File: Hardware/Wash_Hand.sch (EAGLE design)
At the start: 91 parts, among them IC1 LM358D, IC2 LP298XS, IC3 405016TSSOP, J1 I2C, J2 ICSP, J3 SPI, J4 9V_CONN, J5 EXT_VCC, J6 6_PIN_SERIAL_CABLEPTH, J7 OP_B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

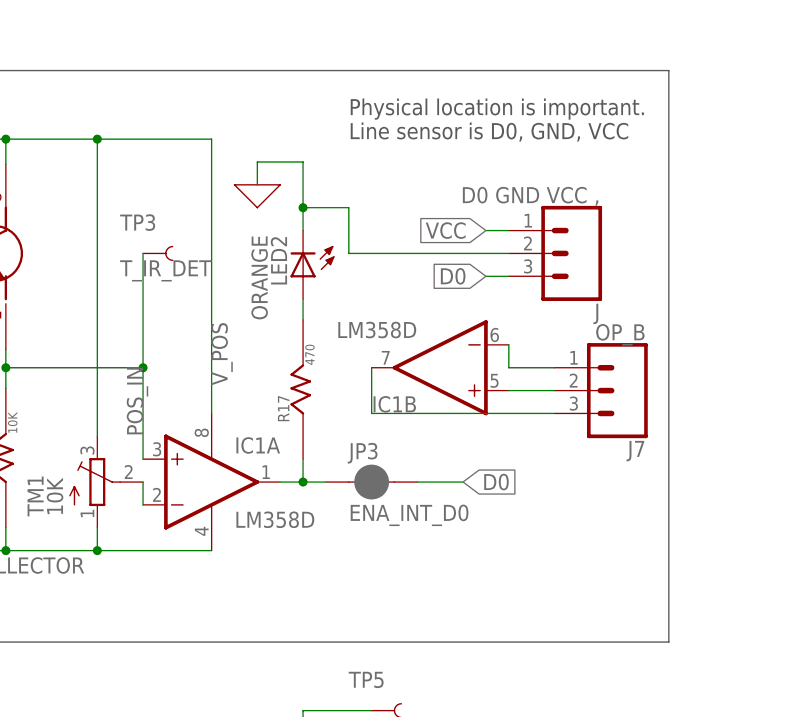
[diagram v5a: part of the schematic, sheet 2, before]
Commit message: Board/Schematic: Route Orange LED2 to NPN_COLLECTOR
instead of the common ground. This way when we disable
the ON_OFF_SWT the light will not be light up.

Signed-off-by: Konrad Rzeszutek Wilk <konrad@kernel.org>
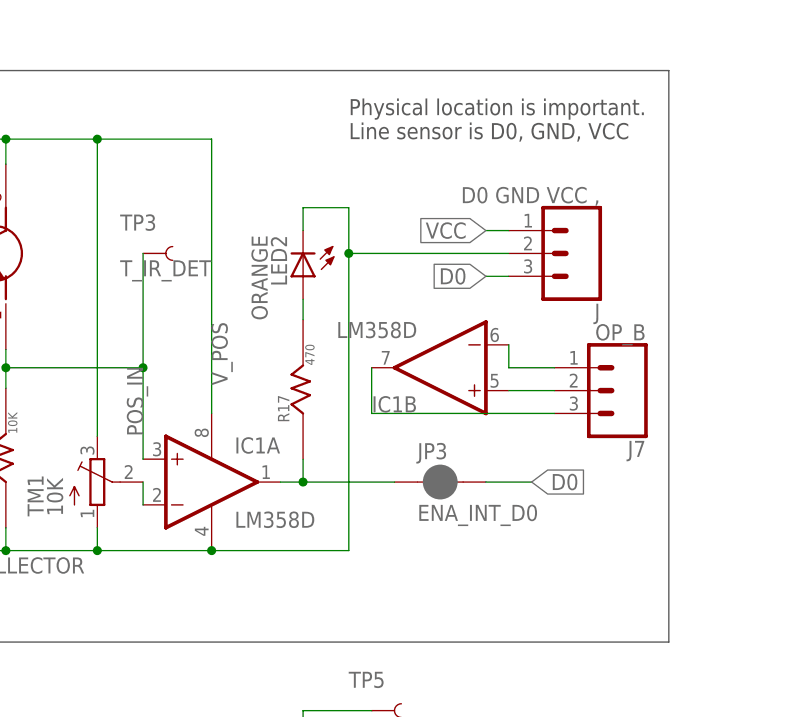
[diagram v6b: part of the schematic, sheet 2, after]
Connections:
- net 0: no longer J.2, LED2.C
- net NPN_COLLECTOR: now also J.2, LED2.C
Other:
- moved on the sheet: JP3
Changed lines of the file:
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@@
 <part name="LOGO2" library="darnok_logo" deviceset="HAPPY_FACE_LOGO" device=""/>
 <part name="X_1" library="ngspice-simulation" library_urn="urn:adsk.eagle:library:527439" deviceset="GND" device=""/>
-<part name="X_4" library="ngspice-simulation" library_urn="urn:adsk.eagle:library:527439" deviceset="GND" device=""/>
 <part name="JP7" library="SparkFun-Jumpers" library_urn="urn:adsk.eagle:library:528" deviceset="JUMPER-SMT_2_NO" device="_SILK" package3d_urn="urn:adsk.eagle:package:39279/1" value="BYPASS_SWT"/>
 </parts>
@@
 <attribute name="NAME" x="233.68" y="151.892" size="1.778" layer="95" font="vector" rot="R180"/>
 </instance>
-<instance part="JP3" gate="G$1" x="208.28" y="132.08" smashed="yes">
-<attribute name="NAME" x="205.74" y="134.62" size="1.778" layer="95" font="vector"/>
-<attribute name="VALUE" x="205.74" y="129.54" size="1.778" layer="96" font="vector" align="top-left"/>
+<instance part="JP3" gate="G$1" x="215.9" y="132.08" smashed="yes">
+<attribute name="NAME" x="213.36" y="134.62" size="1.778" layer="95" font="vector"/>
+<attribute name="VALUE" x="213.36" y="129.54" size="1.778" layer="96" font="vector" align="top-left"/>
 </instance>
 <instance part="JP4" gate="G$1" x="142.24" y="170.18" smashed="yes">
@@
 </instance>
 <instance part="X_1" gate="G$1" x="137.16" y="119.38" smashed="yes"/>
-<instance part="X_4" gate="G$1" x="195.58" y="165.1" smashed="yes"/>
 <instance part="JP7" gate="G$1" x="147.32" y="121.92" smashed="yes">
 <attribute name="NAME" x="144.78" y="124.46" size="1.778" layer="95" font="vector"/>
@@
 <junction x="137.16" y="121.92"/>
 </segment>
-<segment>
-<pinref part="X_4" gate="G$1" pin="0"/>
-<wire x1="195.58" y1="165.1" x2="195.58" y2="167.64" width="0.1524" layer="91"/>
-<pinref part="LED2" gate="G$1" pin="C"/>
-<wire x1="195.58" y1="167.64" x2="200.66" y2="167.64" width="0.1524" layer="91"/>
-<wire x1="200.66" y1="167.64" x2="200.66" y2="162.56" width="0.1524" layer="91"/>
-<pinref part="J" gate="J$1" pin="2"/>
-<wire x1="200.66" y1="162.56" x2="200.66" y2="160.02" width="0.1524" layer="91"/>
-<wire x1="223.52" y1="157.48" x2="205.74" y2="157.48" width="0.1524" layer="91"/>
-<wire x1="205.74" y1="157.48" x2="205.74" y2="162.56" width="0.1524" layer="91"/>
-<wire x1="205.74" y1="162.56" x2="200.66" y2="162.56" width="0.1524" layer="91"/>
-<junction x="200.66" y="162.56"/>
-</segment>
 </net>
 <net name="D0" class="0">
@@
 <wire x1="198.12" y1="132.08" x2="200.66" y2="132.08" width="0.1524" layer="91"/>
 <pinref part="R17" gate="G$1" pin="R_1"/>
-<wire x1="200.66" y1="132.08" x2="203.2" y2="132.08" width="0.1524" layer="91"/>
+<wire x1="200.66" y1="132.08" x2="210.82" y2="132.08" width="0.1524" layer="91"/>
 <wire x1="200.66" y1="132.08" x2="200.66" y2="134.62" width="0.1524" layer="91"/>
 <junction x="200.66" y="132.08"/>
@@
 <segment>
 <pinref part="JP3" gate="G$1" pin="2"/>
-<wire x1="213.36" y1="132.08" x2="218.44" y2="132.08" width="0.1524" layer="91"/>
-<label x="218.44" y="132.08" size="1.778" layer="95" xref="yes"/>
+<wire x1="220.98" y1="132.08" x2="226.06" y2="132.08" width="0.1524" layer="91"/>
+<label x="226.06" y="132.08" size="1.778" layer="95" xref="yes"/>
 </segment>
 </net>
@@
 <wire x1="152.4" y1="121.92" x2="154.94" y2="121.92" width="0.1524" layer="91"/>
 <wire x1="154.94" y1="121.92" x2="154.94" y2="124.46" width="0.1524" layer="91"/>
-</segment>
-</net>
+<pinref part="LED2" gate="G$1" pin="C"/>
+<pinref part="J" gate="J$1" pin="2"/>
+<wire x1="200.66" y1="162.56" x2="200.66" y2="160.02" width="0.1524" layer="91"/>
+<wire x1="223.52" y1="157.48" x2="205.74" y2="157.48" width="0.1524" layer="91"/>
+<wire x1="205.74" y1="157.48" x2="205.74" y2="162.56" width="0.1524" layer="91"/>
+<wire x1="205.74" y1="162.56" x2="200.66" y2="162.56" width="0.1524" layer="91"/>
+<wire x1="205.74" y1="157.48" x2="205.74" y2="124.46" width="0.1524" layer="91"/>
+<wire x1="205.74" y1="124.46" x2="190.5" y2="124.46" width="0.1524" layer="91"/>
+<junction x="205.74" y="157.48"/>
+<junction x="190.5" y="124.46"/>
+</segment>
+</net>

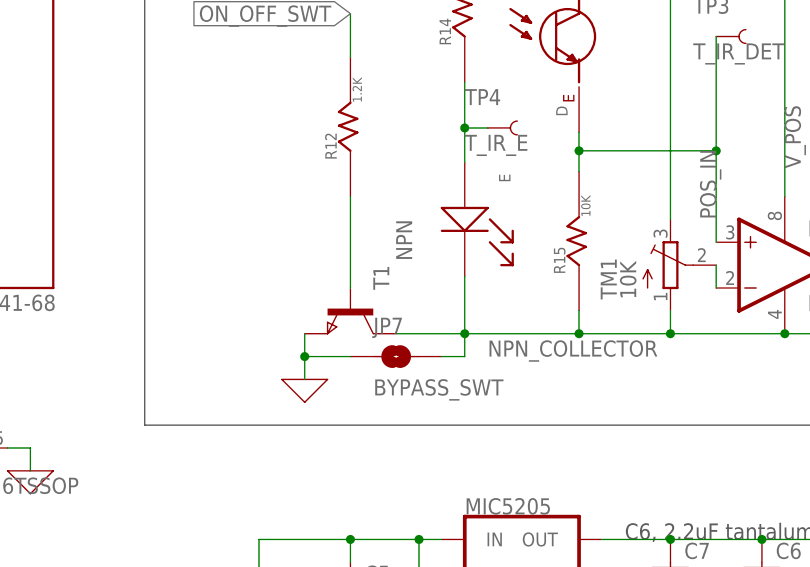
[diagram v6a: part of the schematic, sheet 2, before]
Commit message: Board/Schematic: Add values and move text around a bit
so that it is not over the board.

Signed-off-by: Konrad Rzeszutek Wilk <konrad@kernel.org>
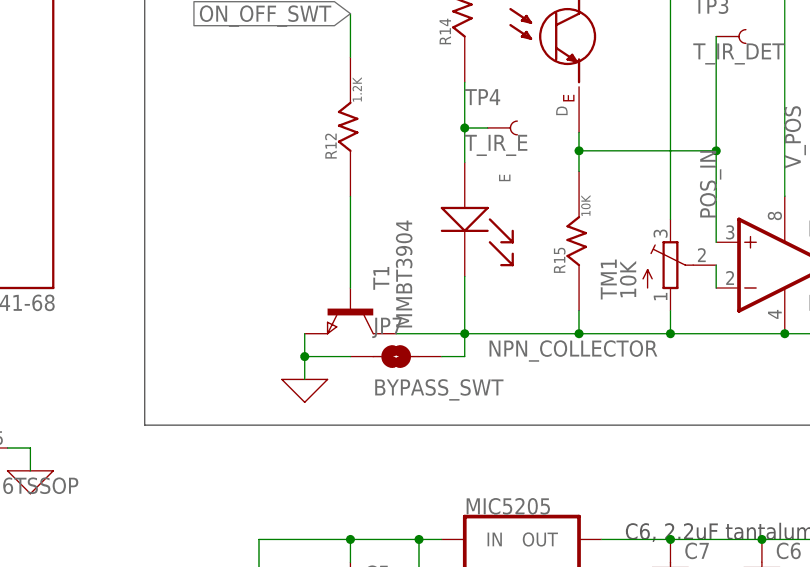
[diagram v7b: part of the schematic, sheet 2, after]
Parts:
- T1: value NPN -> MMBT3904
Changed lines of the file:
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@@
 <part name="X_36" library="ngspice-simulation" library_urn="urn:adsk.eagle:library:527439" deviceset="GND" device=""/>
 <part name="J7" library="SparkFun-Connectors" library_urn="urn:adsk.eagle:library:513" deviceset="CONN_03" device="" package3d_urn="urn:adsk.eagle:package:38063/1" value="OP_B"/>
-<part name="T1" library="zetex" library_urn="urn:adsk.eagle:library:418" deviceset="NPNSOT23" device="" package3d_urn="urn:adsk.eagle:package:30981/1" value="NPN"/>
+<part name="T1" library="zetex" library_urn="urn:adsk.eagle:library:418" deviceset="NPNSOT23" device="" package3d_urn="urn:adsk.eagle:package:30981/1" value="MMBT3904"/>
 <part name="J8" library="SparkFun-Connectors" library_urn="urn:adsk.eagle:library:513" deviceset="CONN_06X2" device="PTH_FEMALE" package3d_urn="urn:adsk.eagle:package:38277/1" value="2X6 FEMALE"/>
 <part name="R12" library="darnok_common" deviceset="RESISTOR" device="R1206" value="1.2K"/>
